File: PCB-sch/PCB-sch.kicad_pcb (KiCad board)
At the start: 2 copper layers, 285.8 x 95.3 mm, 142 parts, among them J1 AVR-ISP-6, SW1 SW_Push, U1 ATmega32U4-A, U2 PRTR5V0U2X, Y1 16MHz

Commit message: test
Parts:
- moved R5 2.25 mm to (75.3, 68.7), turned to -90 degrees
- moved USB1 0.80 mm to (82.4, 62.4)
- moved R4 0.33 mm to (89.1, 70.6)
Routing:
- net GND: track 367.6 -> 376.9 mm
- net +5V: track 339.7 -> 346.5 mm, vias 9 -> 11
- net Net-(USB1-CC1): track 12.3 -> 8.75 mm
- net Net-(USB1-CC2): track 6.86 -> 10.2 mm
- net DN: track 199.0 -> 197.6 mm
- net DP: track 200.6 -> 199.6 mm

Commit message: rerouted vias
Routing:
- net col11: track 169.4 -> 175.6 mm, vias 5 -> 8
- net col0: track 232.8 -> 238.1 mm, vias 8 -> 12
- net col9: track 135.0 -> 139.9 mm, vias 5 -> 8
- net col13: track 237.9 -> 242.8 mm, vias 5 -> 0
- net col10: track 156.7 -> 160.1 mm, vias 6 -> 10
- net col8: track 124.3 -> 127.7 mm, vias 5 -> 8
- net col3: track 153.8 -> 157.1 mm, vias 9 -> 12
- net col2: track 184.5 -> 187.7 mm, vias 7 -> 10
- net +5V: track 346.5 -> 343.5 mm
- net col7: track 99.4 -> 101.9 mm, vias 5 -> 8
- net col6: track 110.0 -> 112.2 mm, vias 5 -> 8
- net GND: track 376.9 -> 378.6 mm
- net col5: track 107.8 -> 109.0 mm, vias 9 -> 12
- net row1: track 314.8 -> 313.7 mm
- net col4: track 129.4 -> 130.2 mm, vias 9 -> 12
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- added copper zone on B.Cu, net GND
- added copper zone on F.Cu, net GND

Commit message: rerouted vias
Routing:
- net col12: track 207.8 -> 210.8 mm, vias 4 -> 6
- removed copper zone on F.Cu, net GND

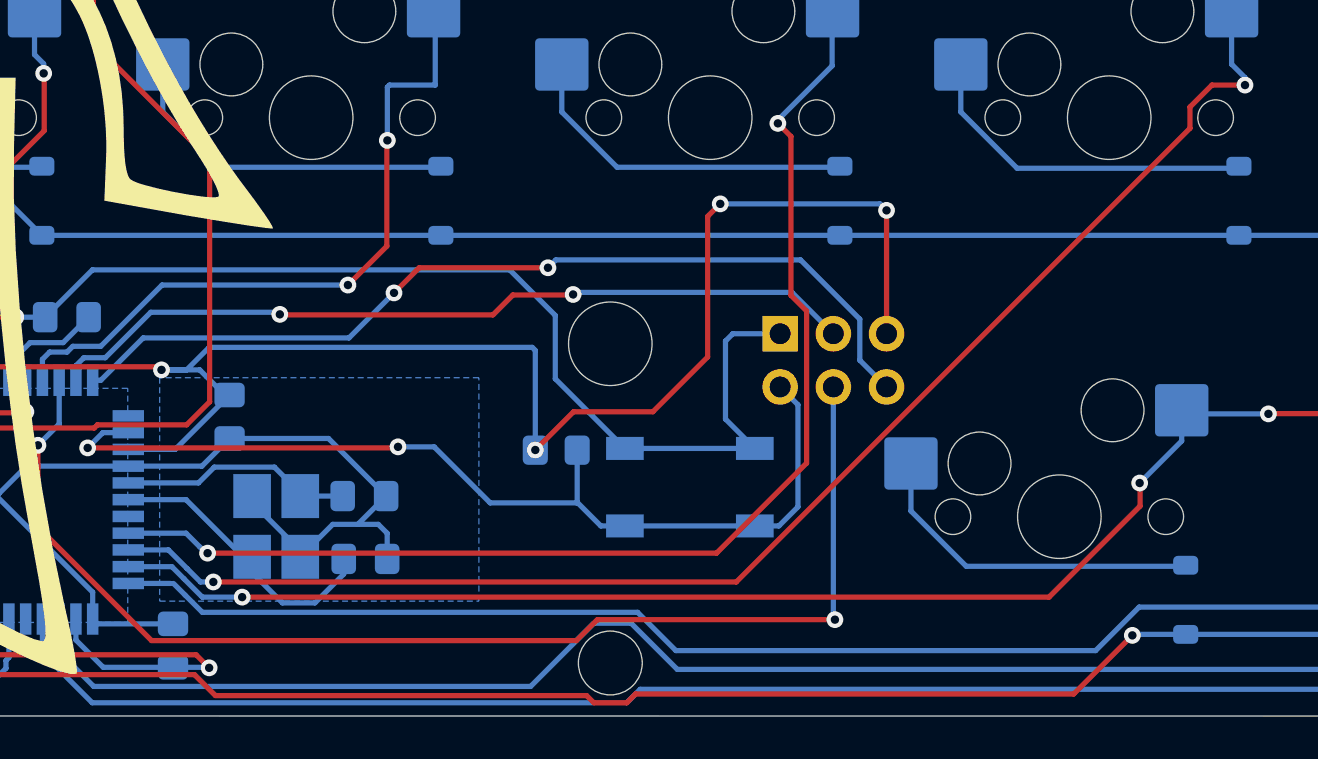
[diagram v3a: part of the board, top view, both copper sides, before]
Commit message: rerouted vias
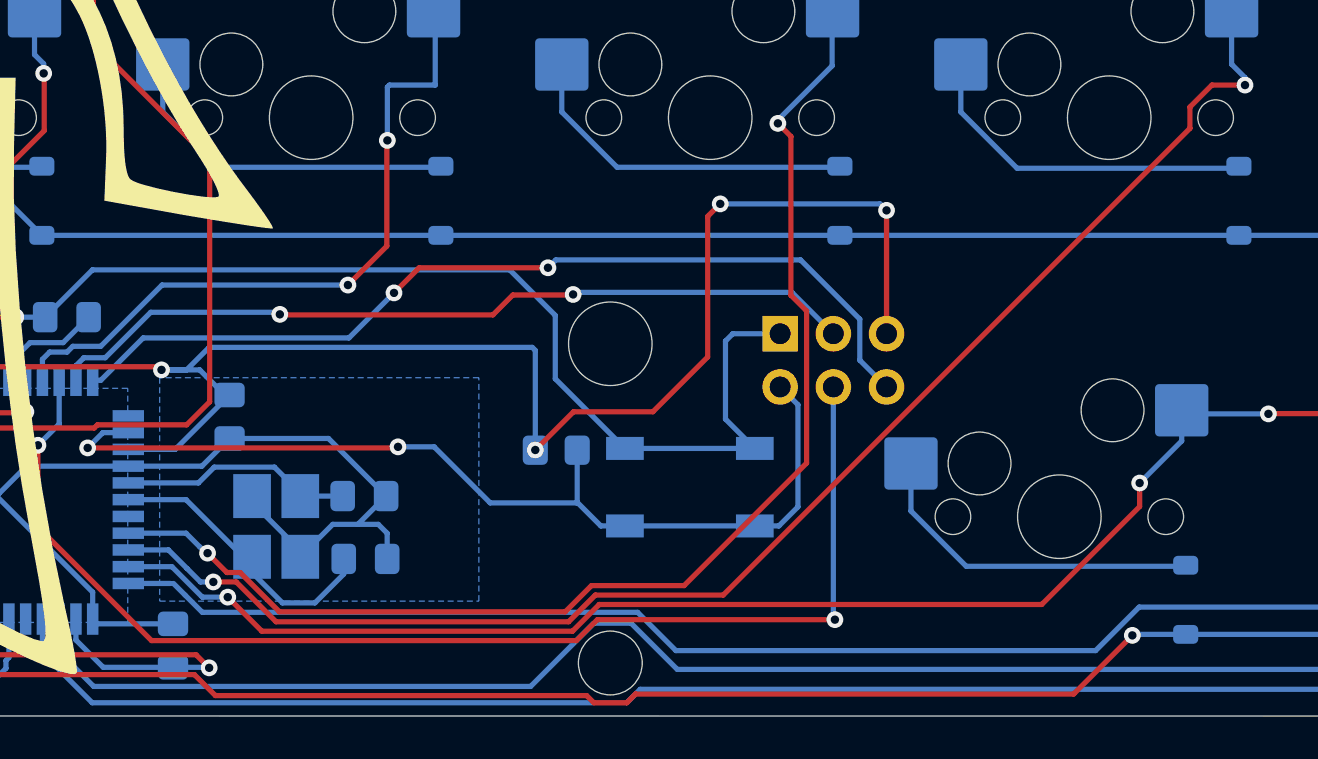
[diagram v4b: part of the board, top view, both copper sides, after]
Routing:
- net col8: track 127.7 -> 130.0 mm
- net col9: track 139.9 -> 141.5 mm
- net col10: track 160.1 -> 161.5 mm

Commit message: rerouted vias
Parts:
- added REF**: MountingHole_2.2mm_M2_Pad, MountingHole:MountingHole_2.2mm_M2_Pad, F.Cu at (65.0, 120.1)
- added REF**: MountingHole_2.2mm_M2_Pad, MountingHole:MountingHole_2.2mm_M2_Pad, F.Cu at (348.0, 120.1)
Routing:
- net GND: vias 4 -> 6
- added copper zone on F.Cu, net GND
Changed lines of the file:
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@@
 			(drillshape 0)
 			(scaleselection 1)
-			(outputdirectory "../Manufacturing/")
+			(outputdirectory "C:/Users/djack/60-PCB/Final Manu/")
 		)
 	)
@@
 	(net 102 "DN")
 	(net 103 "DP")
+	(footprint "MountingHole:MountingHole_2.2mm_M2_Pad"
+		(layer "F.Cu")
+		(at 65 120.1)
+		(descr "Mounting Hole 2.2mm, M2")
+		(tags "mounting hole 2.2mm m2")
+		(property "Reference" "REF**"
+			(at 0 -3.2 0)
+			(layer "F.SilkS")
+			(effects
+				(font
+					(size 1 1)
+					(thickness 0.15)
+				)
+			)
+		)
+		(property "Value" "MountingHole_2.2mm_M2_Pad"
+			(at 0 3.2 0)
+			(layer "F.Fab")
+			(hide yes)
+			(effects
+				(font
+					(size 1 1)
+					(thickness 0.15)
+				)
+			)
+		)
+		(property "Footprint" "MountingHole:MountingHole_2.2mm_M2_Pad"
+			(at 0 0 0)
+			(unlocked yes)
+			(layer "F.Fab")
+			(hide yes)
+			(effects
+				(font
+					(size 1.27 1.27)
+					(thickness 0.15)
+				)
+			)
+		)
+		(property "Datasheet" ""
+			(at 0 0 0)
+			(unlocked yes)
+			(layer "F.Fab")
+			(hide yes)
+			(effects
+				(font
+					(size 1.27 1.27)
+					(thickness 0.15)
+				)
+			)
+		)
+		(property "Description" ""
+			(at 0 0 0)
+			(unlocked yes)
+			(layer "F.Fab")
+			(hide yes)
+			(effects
+				(font
+					(size 1.27 1.27)
+					(thickness 0.15)
+				)
+			)
+		)
+		(attr exclude_from_pos_files exclude_from_bom)
+		(pad "2" thru_hole oval
+			(at 0 0)
+			(size 7 3)
+			(drill oval 6 2.2)
+			(layers "*.Cu" "*.Mask")
+			(remove_unused_layers no)
+		)
+	)
+	(footprint "MountingHole:MountingHole_2.2mm_M2_Pad"
+		(layer "F.Cu")
+		(at 348 120.1)
+		(descr "Mounting Hole 2.2mm, M2")
+		(tags "mounting hole 2.2mm m2")
+		(property "Reference" "REF**"
+			(at 0 -3.2 0)
+			(layer "F.SilkS")
+			(effects
+				(font
+					(size 1 1)
+					(thickness 0.15)
+				)
+			)
+		)
+		(property "Value" "MountingHole_2.2mm_M2_Pad"
+			(at 0 3.2 0)
+			(layer "F.Fab")
+			(hide yes)
+			(effects
+				(font
+					(size 1 1)
+					(thickness 0.15)
+				)
+			)
+		)
+		(property "Footprint" "MountingHole:MountingHole_2.2mm_M2_Pad"
+			(at 0 0 0)
+			(unlocked yes)
+			(layer "F.Fab")
+			(hide yes)
+			(effects
+				(font
+					(size 1.27 1.27)
+					(thickness 0.15)
+				)
+			)
+		)
+		(property "Datasheet" ""
+			(at 0 0 0)
+			(unlocked yes)
+			(layer "F.Fab")
+			(hide yes)
+			(effects
+				(font
+					(size 1.27 1.27)
+					(thickness 0.15)
+				)
+			)
+		)
+		(property "Description" ""
+			(at 0 0 0)
+			(unlocked yes)
+			(layer "F.Fab")
+			(hide yes)
+			(effects
+				(font
+					(size 1.27 1.27)
+					(thickness 0.15)
+				)
+			)
+		)
+		(attr exclude_from_pos_files exclude_from_bom)
+		(pad "2" thru_hole oval
+			(at 0 0)
+			(size 7 3)
+			(drill oval 6 2.2)
+			(layers "*.Cu" "*.Mask")
+			(remove_unused_layers no)
+		)
+	)
 	(footprint "Resistor_SMD:R_0805_2012Metric_Pad1.20x1.40mm_HandSolder"
 		(layer "B.Cu")
@@
 	)
 	(via
+		(at 235.3 151.4)
+		(size 0.8)
+		(drill 0.4)
+		(layers "F.Cu" "B.Cu")
+		(free yes)
+		(net 1)
+	)
+	(via
 		(at 216.15 139.85)
 		(size 0.8)
@@
 		(net 1)
 	)
+	(via
+		(at 235.38 148.38)
+		(size 0.8)
+		(drill 0.4)
+		(layers "F.Cu" "B.Cu")
+		(free yes)
+		(net 1)
+	)
 	(segment
 		(start 233.875 151.4)
@@
 	)
 	(zone
+		(net 1)
+		(net_name "GND")
+		(layer "F.Cu")
+		(hatch edge 0.5)
+		(priority 4)
+		(connect_pads
+			(clearance 0.5)
+		)
+		(min_thickness 0.25)
+		(filled_areas_thickness no)
+		(fill yes
+			(thermal_gap 0.5)
+			(thermal_bridge_width 0.5)
+		)
+		(polygon
+			(pts
+				(xy 223.01 146.69) (xy 220.76 146.68) (xy 220.76 148.85) (xy 223 148.85) (xy 223.01 146.7)
+			)
+		)
+	)
+	(zone
+		(net 1)
+		(net_name "GND")
+		(layer "F.Cu")
+		(hatch edge 0.5)
+		(priority 3)
+		(connect_pads
+			(clearance 0.5)
+		)
+		(min_thickness 0.25)
+		(filled_areas_thickness no)
+		(fill yes
+			(thermal_gap 0.5)
+			(thermal_bridge_width 0.5)
+		)
+		(polygon
+			(pts
+				(xy 238.27 142.75) (xy 238.26 153.42) (xy 223.01 153.41) (xy 223.02 142.75) (xy 238.28 142.75)
+			)
+		)
+	)
+	(zone

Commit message: final edits
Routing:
- net GND: vias 6 -> 7
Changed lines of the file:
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@@
 			(at 0 -3.2 0)
 			(layer "F.SilkS")
+			(hide yes)
 			(effects
 				(font
@@
 			(at 0 -3.2 0)
 			(layer "F.SilkS")
+			(hide yes)
 			(effects
 				(font
@@
 	)
 	(via
+		(at 225.7 148.45)
+		(size 0.8)
+		(drill 0.4)
+		(layers "F.Cu" "B.Cu")
+		(free yes)
+		(net 1)
+	)
+	(via
 		(at 85.725 80.9625)
 		(size 0.8)
@@
 		(layer "F.Cu")
 		(hatch edge 0.5)
-		(priority 4)
+		(priority 3)
 		(connect_pads
 			(clearance 0.5)
@@
 		(polygon
 			(pts
-				(xy 223.01 146.69) (xy 220.76 146.68) (xy 220.76 148.85) (xy 223 148.85) (xy 223.01 146.7)
+				(xy 238.27 142.75) (xy 238.26 153.42) (xy 223.01 153.41) (xy 223.02 142.75) (xy 238.28 142.75)
 			)
 		)
@@
 		(polygon
 			(pts
-				(xy 238.27 142.75) (xy 238.26 153.42) (xy 223.01 153.41) (xy 223.02 142.75) (xy 238.28 142.75)
+				(xy 223.05 148.9) (xy 220.76 148.97) (xy 220.76 146.61) (xy 223.15 146.61)
 			)
 		)
